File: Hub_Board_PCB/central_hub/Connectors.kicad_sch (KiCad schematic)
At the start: 17 parts, among them J1 CX90B-16P, J10 Conn_02x03_Counter_Clockwise, J4 Conn_02x05_Counter_Clockwise, J4 Screw_Terminal_01x08, J6 Screw_Terminal_01x04, J7 Conn_02x03_Counter_Clockwise, J7 Screw_Terminal_01x14, J8 Conn_01x02, SW1 RotaryEncoder_Switch

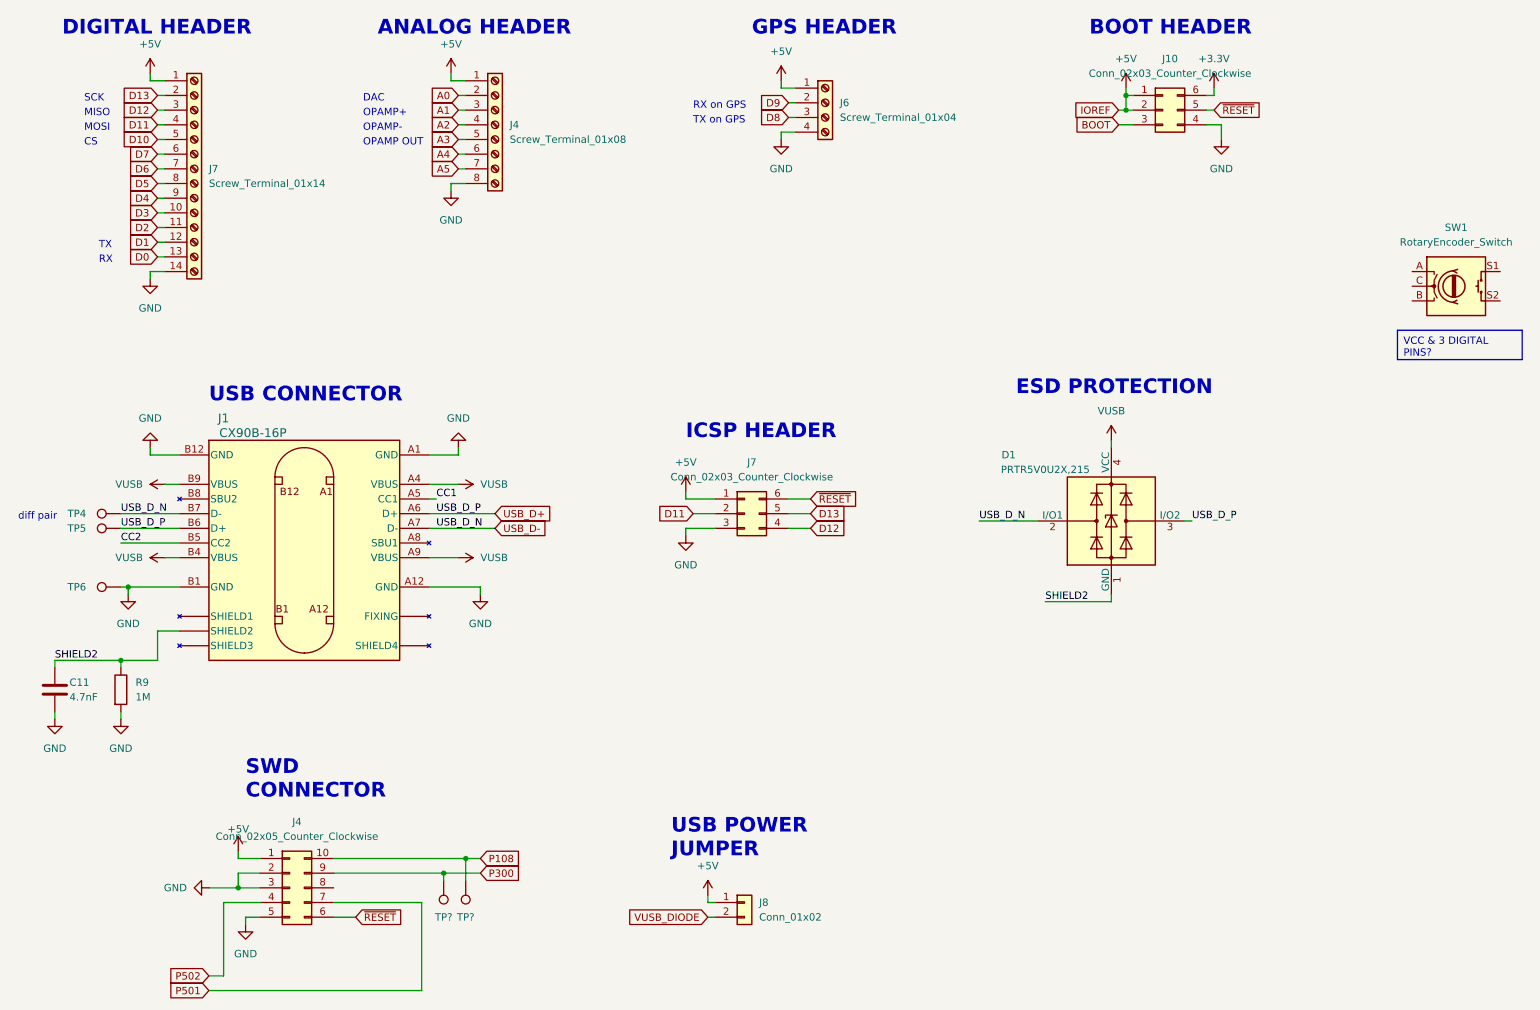
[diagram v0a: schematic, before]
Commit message: Added all other footprints... populated all components with NO errors or warnings :)
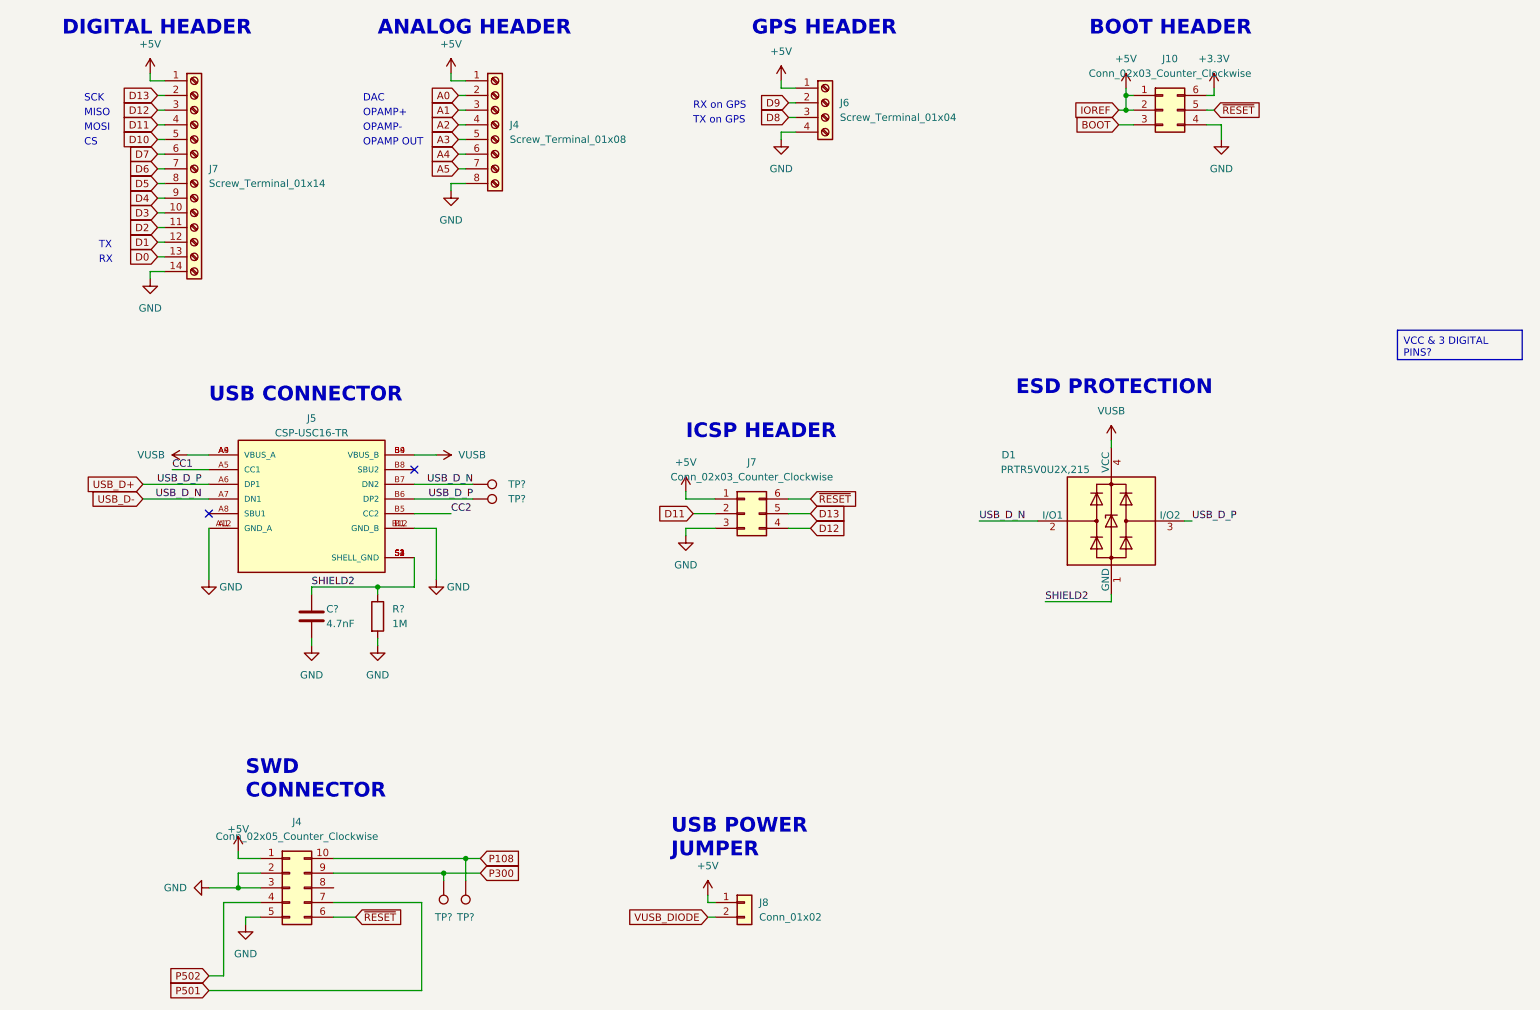
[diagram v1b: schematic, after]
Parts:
- removed C11: 4.7nF, Capacitor_SMD:C_0603_1608Metric, symbol Device:C
- removed J1: CX90B-16P, symbol CX90B-16P:CX90B-16P
- removed R9: 1M, Resistor_SMD:R_0603_1608Metric, symbol Device:R
- removed SW1: RotaryEncoder_Switch, symbol Device:RotaryEncoder_Switch
- removed TP4, TP5, TP6: TestPoint, TestPoint:TestPoint_Pad_D1.0mm, symbol Connector:TestPoint
- added C?: 4.7nF, Capacitor_SMD:C_0603_1608Metric, symbol Device:C
- added J5: CSP-USC16-TR, ~ALL:VALCON_CSP-USC16-TR, symbol CSP-USC16-TR:CSP-USC16-TR
- added R?: 1M, Resistor_SMD:R_0603_1608Metric, symbol Device:R
- added TP? (x2): TestPoint, TestPoint:TestPoint_Pad_D1.0mm, symbol Connector:TestPoint
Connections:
- net CC1: now also J5.A5 (CC1)
- net CC2: now also J5.B5 (CC2)
- net GND: now also C?.1, J5.A1 (GND_A), J5.A12 (GND_A), J5.B1 (GND_B), J5.B12 (GND_B), R?.2
- net SHIELD2: now also C?.2, J5.S1 (SHELL_GND), J5.S2 (SHELL_GND), J5.S3 (SHELL_GND), J5.S4 (SHELL_GND), R?.1
- net USB_D+: now also J5.A6 (DP1), J5.B6 (DP2), TP?.1
- net USB_D-: now also J5.A7 (DN1), J5.B7 (DN2), TP?.1
- net VUSB: now also J5.A4 (VBUS_A), J5.A9 (VBUS_A), J5.B4 (VBUS_B), J5.B9 (VBUS_B)
- no-connect marks 0 -> 2
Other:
- note removed: "diff pair"

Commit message: Fixed header sizes
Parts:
- J6: footprint Connector_PinHeader_2.54mm:PinHeader_1x04_P2.54mm_Horizontal -> Connector_PinHeader_2.54mm:PinHeader_1x04_P2.54mm_Vertical
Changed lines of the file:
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@@
       (effects (font (size 1.27 1.27)) (justify left))
     )
-    (property "Footprint" "Connector_PinHeader_2.54mm:PinHeader_1x04_P2.54mm_Horizontal" (at 156.21 35.56 0)
+    (property "Footprint" "Connector_PinHeader_2.54mm:PinHeader_1x04_P2.54mm_Vertical" (at 156.21 35.56 0)
       (effects (font (size 1.27 1.27)) hide)
     )

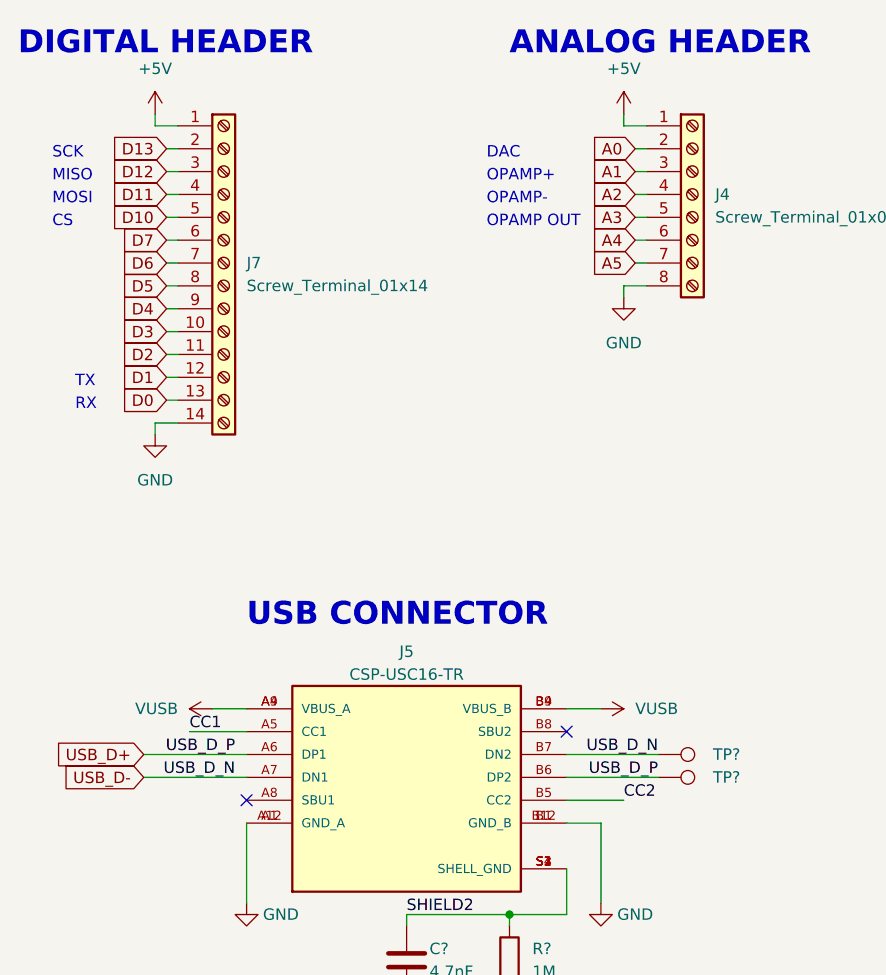
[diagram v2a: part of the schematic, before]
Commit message: Started Layout (hub board)
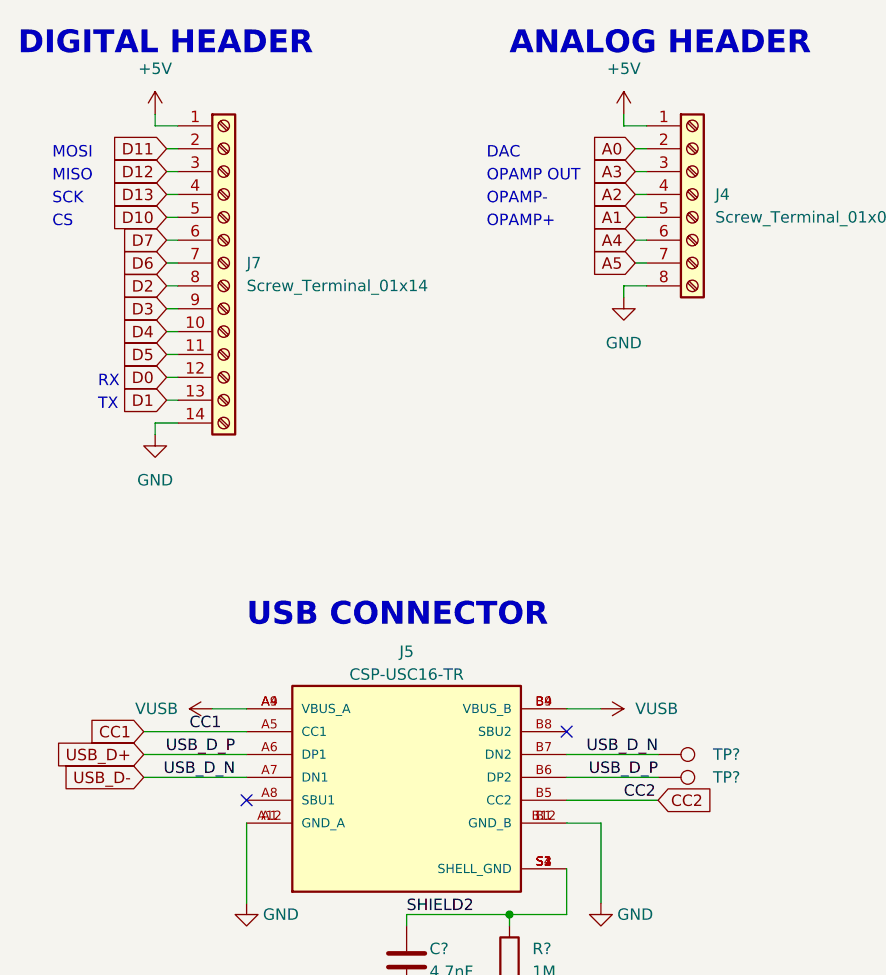
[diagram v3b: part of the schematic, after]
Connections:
- net A1: now also J4.5; no longer J4.3
- net A3: now also J4.3; no longer J4.5
- net D0: now also J7.12; no longer J7.13
- net D1: now also J7.13; no longer J7.12
- net D11: now also J7.2; no longer J7.4
- net D13: now also J7.4; no longer J7.2
- net D2: now also J7.8; no longer J7.11
- net D3: now also J7.9; no longer J7.10
- net D4: now also J7.10; no longer J7.9
- net D5: now also J7.11; no longer J7.8

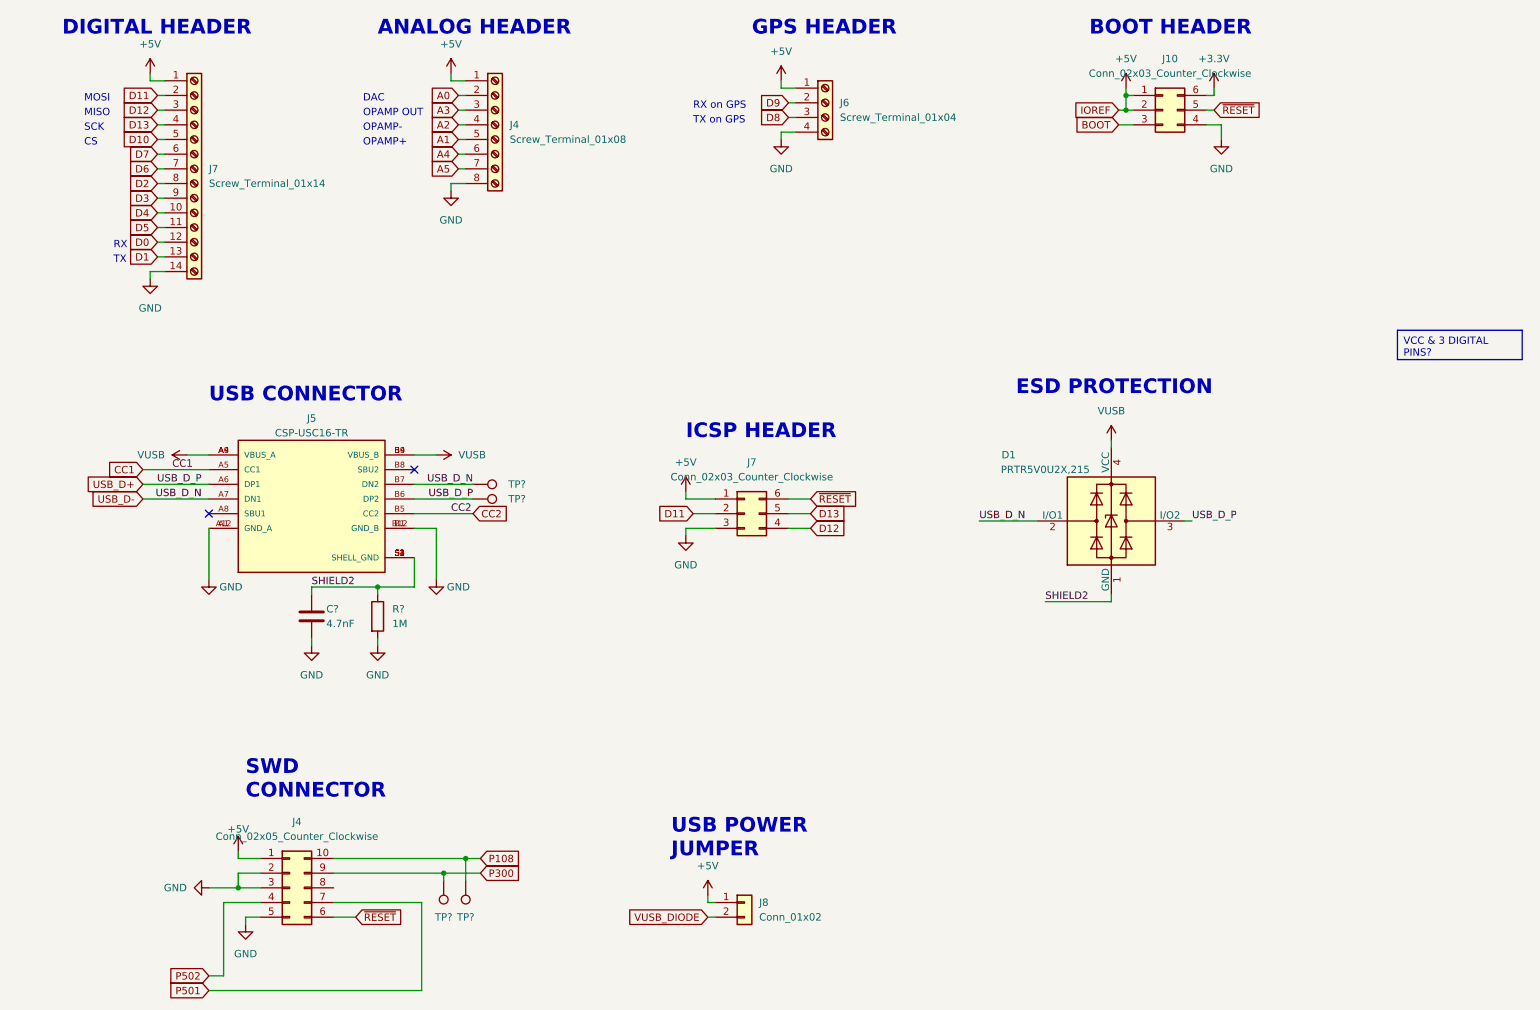
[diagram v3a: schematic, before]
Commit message: Added new connectors as per brandons new shifters
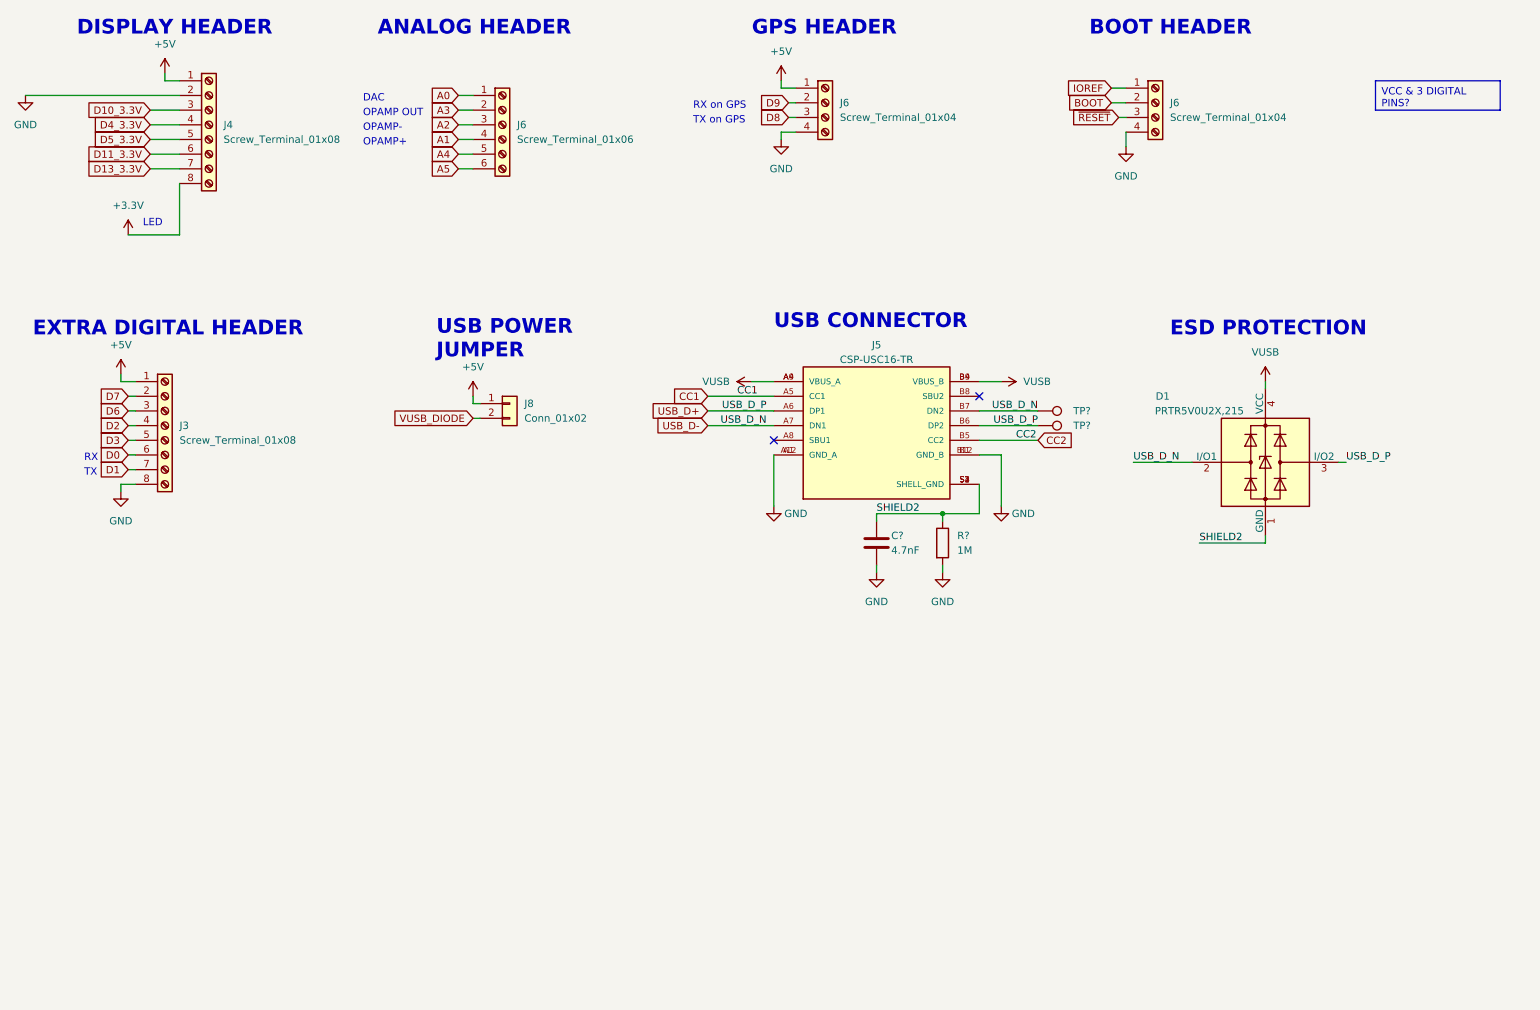
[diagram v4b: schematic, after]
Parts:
- removed J10, J7: Conn_02x03_Counter_Clockwise, Connector_PinHeader_2.54mm:PinHeader_2x03_P2.54mm_Vertical, symbol Connector_Generic:Conn_02x03_Counter_Clockwise
- removed J4: Conn_02x05_Counter_Clockwise, Connector_PinHeader_2.54mm:PinHeader_2x05_P2.54mm_Vertical, symbol Connector_Generic:Conn_02x05_Counter_Clockwise
- removed J7: Screw_Terminal_01x14, Connector_PinHeader_2.54mm:PinHeader_1x14_P2.54mm_Vertical, symbol Connector:Screw_Terminal_01x14
- removed TP? (x2): TestPoint, TestPoint:TestPoint_Pad_D1.0mm, symbol Connector:TestPoint
- added J3: Screw_Terminal_01x08, Connector_PinHeader_2.54mm:PinHeader_1x08_P2.54mm_Vertical, symbol Connector:Screw_Terminal_01x08
- added J6: Screw_Terminal_01x04, Connector_PinHeader_2.54mm:PinHeader_1x04_P2.54mm_Vertical, symbol Connector:Screw_Terminal_01x04
- added J6: Screw_Terminal_01x06, Connector_PinHeader_2.54mm:PinHeader_1x06_P2.54mm_Vertical, symbol Connector:Screw_Terminal_01x06
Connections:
- net +3.3V: now also J4.8 (Pin_8)
- net +5V: now also J3.1 (Pin_1)
- net A0: now also J6.1 (Pin_1); no longer J4.2
- net A1: now also J6.4 (Pin_4); no longer J4.5
- net A2: now also J6.3 (Pin_3); no longer J4.4
- net A3: now also J6.2 (Pin_2); no longer J4.3
- net A4: now also J6.5 (Pin_5); no longer J4.6
- net A5: now also J6.6 (Pin_6); no longer J4.7
- net BOOT: now also J6.2
- net D0: now also J3.6 (Pin_6)
- net D1: now also J3.7 (Pin_7)
- net D2: now also J3.4 (Pin_4)
- net D3: now also J3.5 (Pin_5)
- net D6: now also J3.3 (Pin_3)
- net D7: now also J3.2 (Pin_2)
- net GND: now also J4.2 (Pin_2), J3.8 (Pin_8), J6.4; no longer J4.8
- net ~{RESET}: now also J6.3
- new net D10_3.3V: J4.3 (Pin_3)
- new net D11_3.3V: J4.6 (Pin_6)
- new net D13_3.3V: J4.7 (Pin_7)
- new net D4_3.3V: J4.4 (Pin_4)
- new net D5_3.3V: J4.5 (Pin_5)
- new net IOREF: J6.1
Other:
- note added: "DISPLAY HEADER"
- note added: "EXTRA DIGITAL HEADER"
- note added: "LED"
- note removed: "CS"
- note removed: "DIGITAL HEADER"
- note removed: "ICSP HEADER"
- note removed: "MISO"
- note removed: "MOSI"
- note removed: "SCK"
- note removed: "SWD CONNECTOR"
- moved on the sheet: C?, D1, J5, J8, R?, TP?
